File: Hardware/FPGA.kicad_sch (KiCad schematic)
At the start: 1 part, among them U3 XC7Z010-1CLG225I

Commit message: 11/17 progress update
finished the board, now just need to add the peripheral
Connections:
- net RAM_CLK: now also U3.P13 (IO_L18P_T2_34); no longer U3.L15 (IO_L8P_T1_34)
- net RAM_DQ0: now also U3.R11 (IO_L16N_T2_34); no longer U3.K13 (IO_L10P_T1_34)
- net RAM_DQ1: now also U3.R12 (IO_L17P_T2_34); no longer U3.N11 (IO_L13P_T2_MRCC_34)
- net RAM_DQ2: now also U3.R13 (IO_L17N_T2_34); no longer U3.N14 (IO_L7N_T1_34)
- net RAM_DQ3: now also U3.R10 (IO_L24N_T3_34); no longer U3.P14 (IO_L18N_T2_34)
- net RAM_DQ4: now also U3.R7 (IO_L20P_T3_34); no longer U3.L14 (IO_L9P_T1_DQS_34)
- net RAM_DQ5: now also U3.P9 (IO_L23N_T3_34); no longer U3.J13 (IO_L5P_T0_34)
- net RAM_DQ6: now also U3.P8 (IO_L23P_T3_34); no longer U3.L13 (IO_L10N_T1_34)
- net RAM_DQ7: now also U3.R8 (IO_L20N_T3_34); no longer U3.P11 (IO_L16P_T2_34)
- net RWDS: now also U3.P10 (IO_L24P_T3_34); no longer U3.M14 (IO_L9N_T1_DQS_34)
- net ~{RAM_CLK}: now also U3.P14 (IO_L18N_T2_34); no longer U3.M15 (IO_L8N_T1_34)
- net ~{RAM_CS0}: now also U3.N8 (IO_L22N_T3_34); no longer U3.R7 (IO_L20P_T3_34)
- net ~{RAM_CS1}: now also U3.N9 (IO_L19N_T3_VREF_34); no longer U3.R10 (IO_L24N_T3_34)
- net ~{RAM_RST}: now also U3.P11 (IO_L16P_T2_34); no longer U3.L12 (IO_L12P_T1_MRCC_34)
- net D2-: now reaches U3.G12 (IO_L2P_T0_34)
- net GPIO2: now reaches U3.G14 (IO_L3P_T0_DQS_PUDC_B_34)
- net D2+: now reaches U3.H13 (IO_L2N_T0_34)
- net D0-: now reaches U3.J14 (IO_L5N_T0_34)
- net GPIO5: now reaches U3.K15 (IO_L4N_T0_34)
- net D1+: now reaches U3.M10 (IO_L21P_T3_DQS_34)
- net D1-: now reaches U3.M11 (IO_L21N_T3_DQS_34)
- net CK-: now reaches U3.M12 (IO_L12N_T1_MRCC_34)
- net GPIO11: now reaches U3.P15 (IO_L15P_T2_DQS_34)
- net GPIO12: now reaches U3.R15 (IO_L15N_T2_DQS_34)
- net GPIO24: now reaches U3.F12 (IO_L1P_T0_AD0P_35)
- net GPIO23: now reaches U3.F13 (IO_L3P_T0_DQS_AD1P_35)
- net GPIO22: now reaches U3.F14 (IO_L3N_T0_DQS_AD1N_35)
- net GPIO21: now reaches U3.F15 (IO_L5N_T0_AD9N_35)
- new net CK+: U3.L12 (IO_L12P_T1_MRCC_34)
- new net D0+: U3.J13 (IO_L5P_T0_34)
- new net GPIO10: U3.M15 (IO_L8N_T1_34)
- new net GPIO18: U3.N14 (IO_L7N_T1_34)
- new net GPIO19: U3.M14 (IO_L9N_T1_DQS_34)
- new net GPIO20: U3.L15 (IO_L8P_T1_34)
- new net GPIO25: U3.K13 (IO_L10P_T1_34)
- new net GPIO3: U3.L13 (IO_L10N_T1_34)
- new net GPIO4: U3.L14 (IO_L9P_T1_DQS_34)
- no-connect marks 0 -> 52

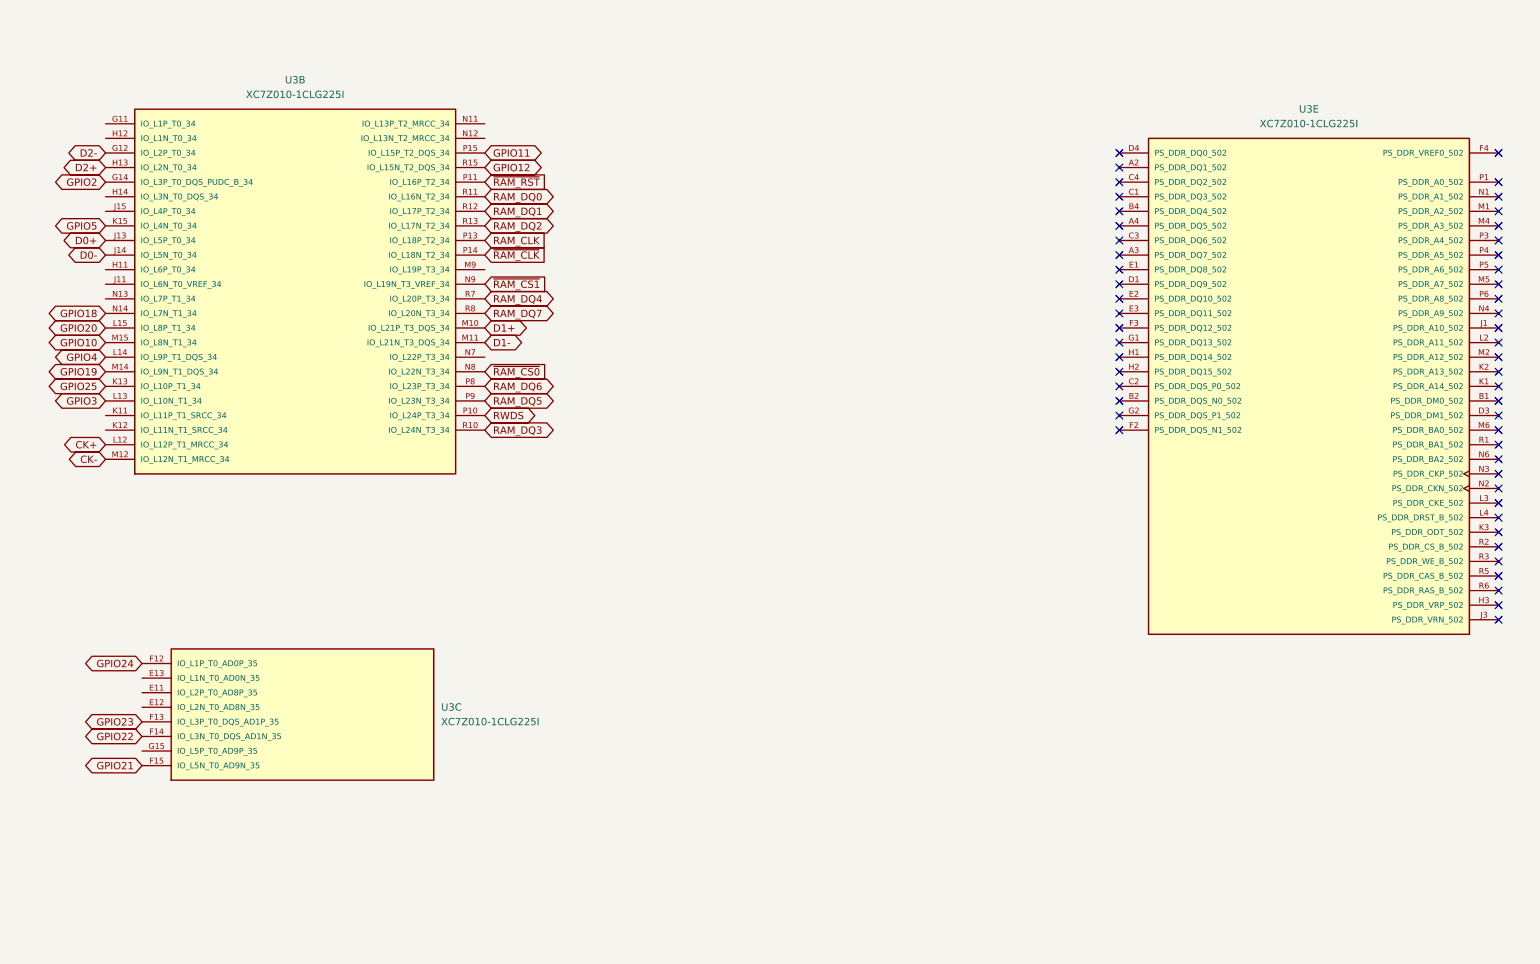
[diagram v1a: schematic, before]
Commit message: 11/19 update
add new header for jtag and fixed a couple of small things
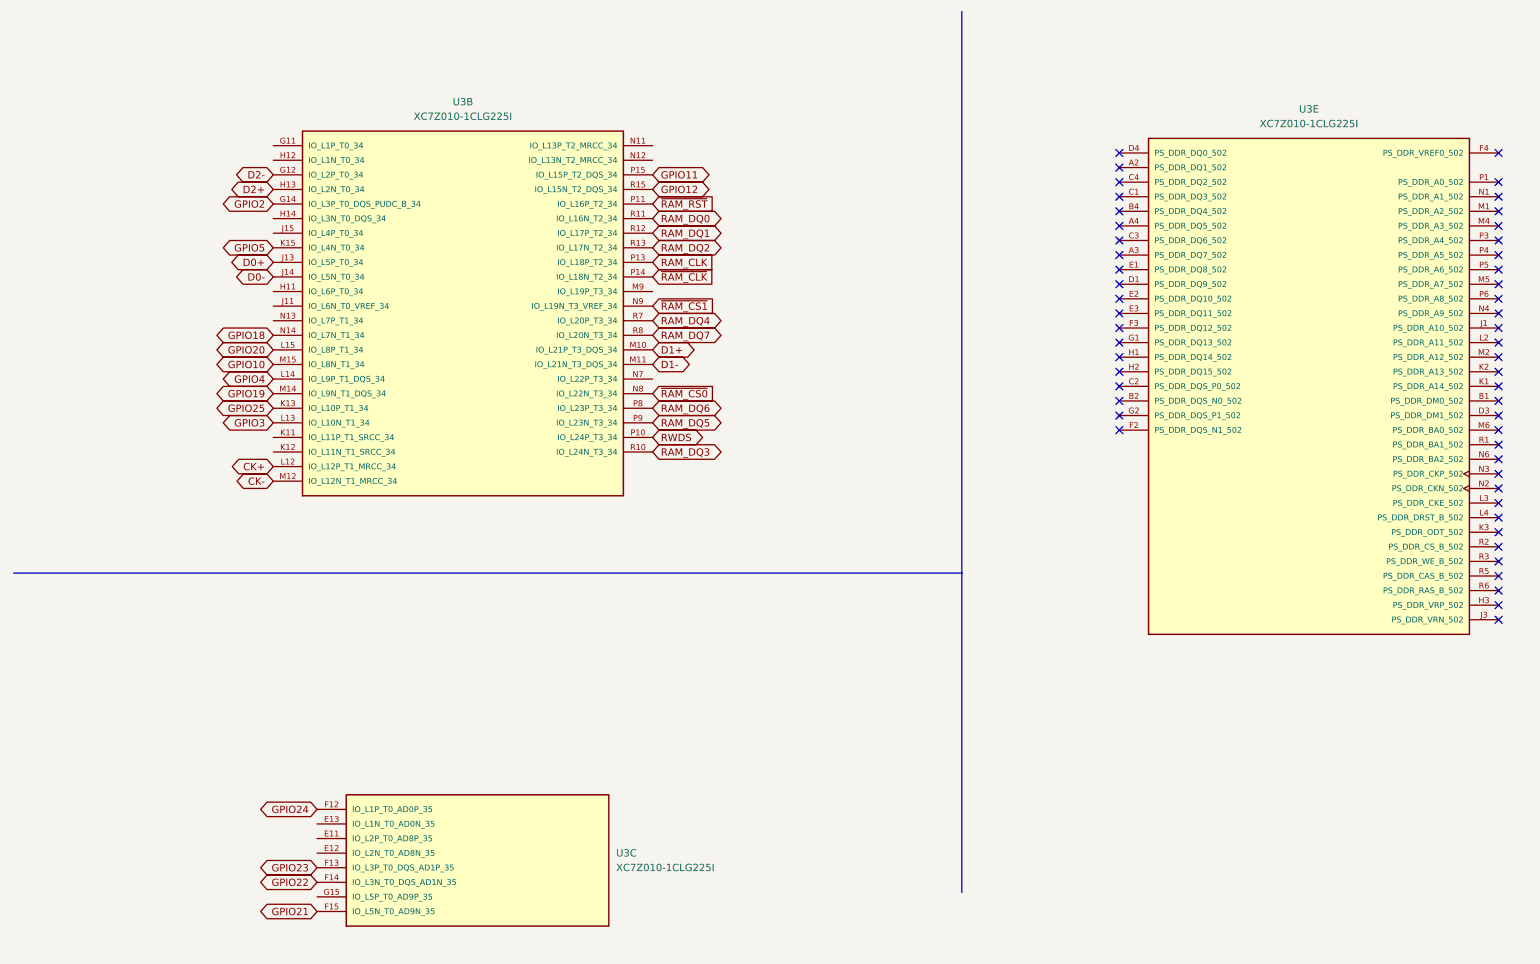
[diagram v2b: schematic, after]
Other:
- moved on the sheet: U3B, U3C

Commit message: 11/21 update
finished annotating the schematic and add pictures and output the pdf
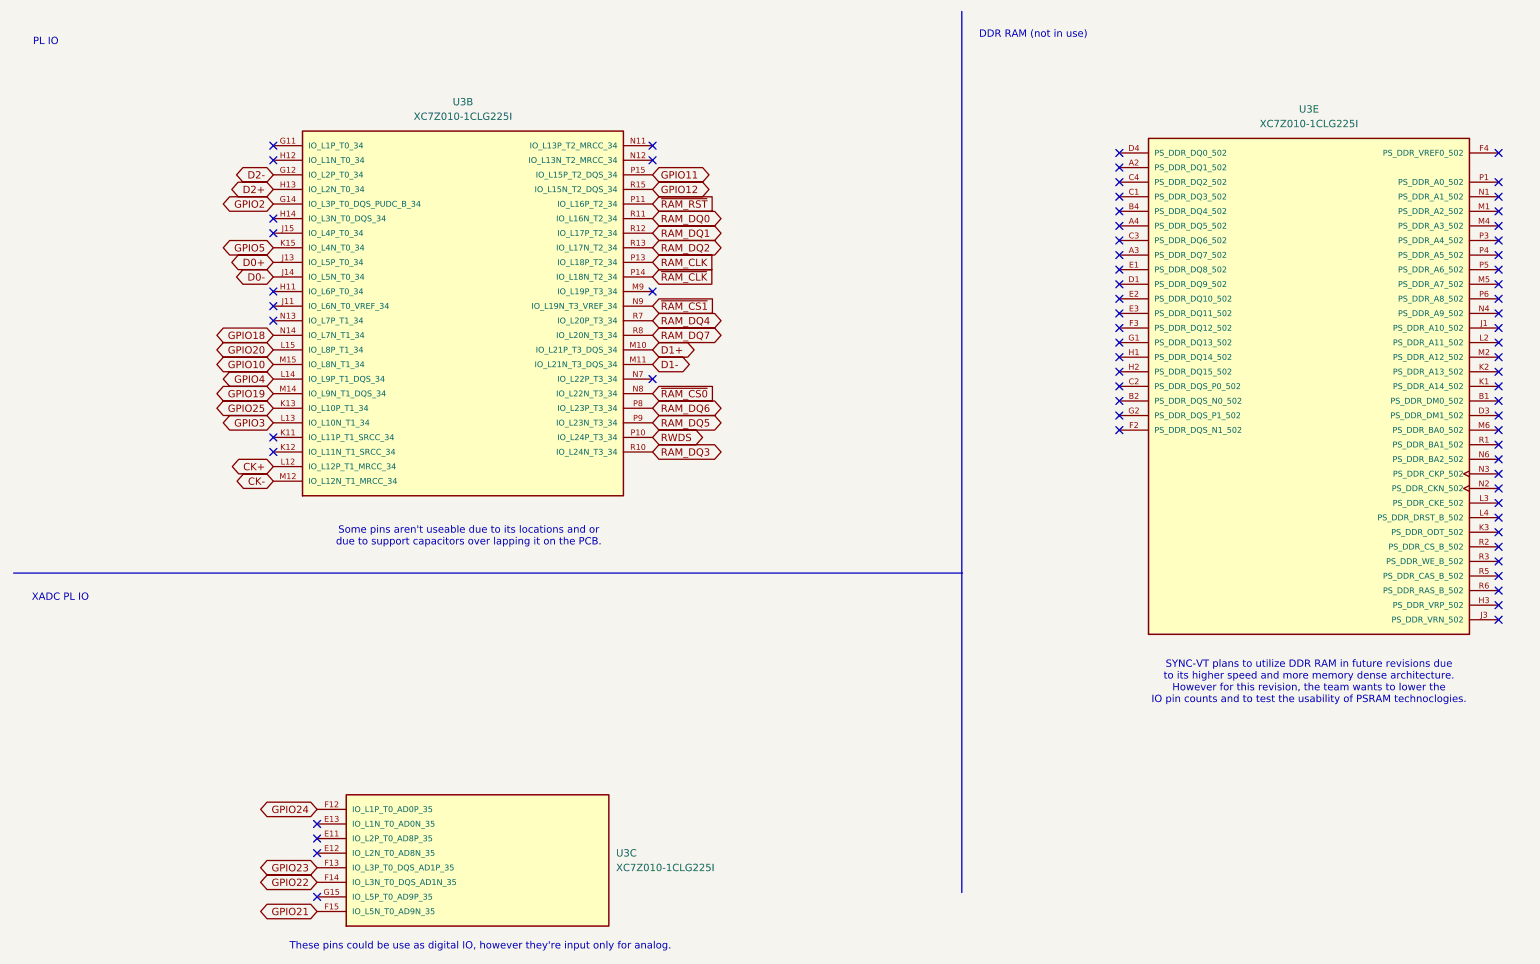
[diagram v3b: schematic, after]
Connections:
- no-connect marks 52 -> 69
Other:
- note added: "DDR RAM (not in use)"
- note added: "PL IO"
- note added: "SYNC-VT plans to utilize DDR RAM in future revisions due to its higher speed and more memory dense architecture. However for this revision, the team wants to lower the IO pin counts and to test the usability of PSRAM technoclogies."
- note added: "Some pins aren't useable due to its locations and or due to support capacitors over lapping it on the PCB."
- note added: "These pins could be use as digital IO, however they're input only for analog."
- note added: "XADC PL IO"
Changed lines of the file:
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@@
 	(paper "A4")
 	(no_connect
+		(at 64.77 156.21)
+	)
+	(no_connect
+		(at 57.15 63.5)
+	)
+	(no_connect
 		(at 204.47 49.53)
 	)
@@
 	)
 	(no_connect
+		(at 123.19 76.2)
+	)
+	(no_connect
 		(at 270.51 82.55)
 	)
@@
 	)
 	(no_connect
+		(at 57.15 86.36)
+	)
+	(no_connect
 		(at 204.47 85.09)
 	)
@@
 	)
 	(no_connect
+		(at 64.77 158.75)
+	)
+	(no_connect
 		(at 270.51 80.01)
 	)
@@
 	)
 	(no_connect
+		(at 57.15 50.8)
+	)
+	(no_connect
 		(at 204.47 62.23)
 	)
@@
 	)
 	(no_connect
+		(at 57.15 38.1)
+	)
+	(no_connect
 		(at 270.51 64.77)
 	)
@@
 	)
 	(no_connect
+		(at 57.15 35.56)
+	)
+	(no_connect
 		(at 270.51 97.79)
 	)
@@
 	)
 	(no_connect
+		(at 57.15 88.9)
+	)
+	(no_connect
 		(at 270.51 44.45)
 	)
@@
 	)
 	(no_connect
+		(at 64.77 153.67)
+	)
+	(no_connect
 		(at 270.51 105.41)
 	)
@@
 	)
 	(no_connect
+		(at 123.19 60.96)
+	)
+	(no_connect
 		(at 204.47 57.15)
 	)
@@
 	)
 	(no_connect
+		(at 64.77 166.37)
+	)
+	(no_connect
 		(at 270.51 36.83)
 	)
@@
 	)
 	(no_connect
+		(at 123.19 35.56)
+	)
+	(no_connect
 		(at 270.51 92.71)
 	)
@@
 	)
 	(no_connect
+		(at 57.15 66.04)
+	)
+	(no_connect
 		(at 204.47 59.69)
 	)
@@
 	)
 	(no_connect
+		(at 123.19 38.1)
+	)
+	(no_connect
+		(at 57.15 60.96)
+	)
+	(no_connect
 		(at 270.51 107.95)
 	)
@@
 	(no_connect
 		(at 270.51 87.63)
+	)
+	(no_connect
+		(at 57.15 48.26)
 	)
 	(no_connect
@@
 		)
 	)
+	(text "Some pins aren't useable due to its locations and or\ndue to support capacitors over lapping it on the PCB. "
+		(exclude_from_sim no)
+		(at 91.186 103.632 0)
+		(effects
+			(font
+				(size 1.27 1.27)
+			)
+		)
+	)
+	(text "PL IO"
+		(exclude_from_sim no)
+		(at 17.526 17.526 0)
+		(effects
+			(font
+				(size 1.27 1.27)
+			)
+		)
+	)
+	(text "These pins could be use as digital IO, however they're input only for analog. "
+		(exclude_from_sim no)
+		(at 93.218 175.006 0)
+		(effects
+			(font
+				(size 1.27 1.27)
+			)
+		)
+	)
+	(text "DDR RAM (not in use)"
+		(exclude_from_sim no)
+		(at 189.484 16.256 0)
+		(effects
+			(font
+				(size 1.27 1.27)
+			)
+		)
+	)
+	(text "SYNC-VT plans to utilize DDR RAM in future revisions due \nto its higher speed and more memory dense architecture. \nHowever for this revision, the team wants to lower the\nIO pin counts and to test the usability of PSRAM technoclogies. "
+		(exclude_from_sim no)
+		(at 237.49 129.032 0)
+		(effects
+			(font
+				(size 1.27 1.27)
+			)
+		)
+	)
+	(text "XADC PL IO"
+		(exclude_from_sim no)
+		(at 20.066 114.3 0)
+		(effects
+			(font
+				(size 1.27 1.27)
+			)
+		)
+	)
